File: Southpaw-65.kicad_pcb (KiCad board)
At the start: 2 copper layers, 204 parts, among them J1 USB_C_Receptacle_USB2.0, SW1 SW_Push, U1 ATmega32A-PU, Y1 16MHz

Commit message: Added more diodes into the matrix
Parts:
- moved D0-16 306.8 mm to (420.7, 61.9), turned to 270 degrees
- moved D3-3 282.8 mm to (150.0, 47.6), turned to 270 degrees
- moved D0-11 279.4 mm to (325.4, 61.9), turned to 270 degrees
- moved D0-8 278.8 mm to (268.3, 61.9), turned to 270 degrees
- moved D1-6 270.6 mm to (234.2, 57.1), turned to 270 degrees
- moved D1-7 270.2 mm to (253.2, 57.1), turned to 270 degrees
- moved D0-4 267.8 mm to (192.1, 61.9), turned to 270 degrees
- moved D0-12 266.2 mm to (344.5, 61.9), turned to 270 degrees
- moved D0-10 257.9 mm to (306.4, 61.9), turned to 270 degrees
- moved D1-12 248.2 mm to (348.5, 57.1), turned to 270 degrees
- moved D1-3 245.3 mm to (142.1, 57.1), turned to 270 degrees
- moved D0-5 242.8 mm to (211.1, 61.9), turned to 270 degrees
- moved D1-4 235.9 mm to (196.1, 57.1), turned to 270 degrees
- moved D0-19 230.0 mm to (477.8, 61.9), turned to 270 degrees
- moved D0-6 229.3 mm to (230.2, 61.9), turned to 270 degrees
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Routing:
- net ROW4: track 38.1 -> 57.2 mm
- net ROW3: track 38.1 -> 57.2 mm
- net ROW2: track 38.1 -> 57.2 mm
- net ROW1: track 38.1 -> 57.2 mm
- net ROW0: track 38.1 -> 57.2 mm

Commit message: Finished Diode Matrix
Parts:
- moved D3-19 297.7 mm to (451.6, 47.6), turned to 270 degrees
- moved D2-6 294.2 mm to (238.1, 52.4), turned to 270 degrees
- moved D2-7 287.3 mm to (257.2, 52.4), turned to 270 degrees
- moved D4-8 279.2 mm to (280.2, 47.6), turned to 270 degrees
- moved D4-14 275.7 mm to (386.6, 57.1), turned to 270 degrees
- moved D3-12 275.4 mm to (344.5, 61.9), turned to 270 degrees
- moved D3-8 265.9 mm to (276.2, 52.4), turned to 270 degrees
- moved D4-12 263.7 mm to (348.5, 57.1), turned to 270 degrees
- moved D2-5 259.2 mm to (218.3, 52.4), turned to 270 degrees
- moved D2-10 258.7 mm to (306.4, 61.9), turned to 270 degrees
- moved D4-13 258.3 mm to (368.3, 57.1), turned to 270 degrees
- moved D4-10 255.8 mm to (314.3, 52.4), turned to 270 degrees
- moved D2-8 229.3 mm to (272.3, 57.1), turned to 270 degrees
- moved D3-13 226.7 mm to (364.3, 61.9), turned to 270 degrees
- moved D2-18 219.1 mm to (429.4, 52.4), turned to 270 degrees
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
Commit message: More diodes
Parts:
- moved SW1 394.9 mm to (466.6, 46.2)
- moved C6 341.2 mm to (171.3, 76.2)
- moved C3 339.9 mm to (171.3, 84.1)
- moved C7 329.7 mm to (179.3, 84.1)
- moved R6 314.5 mm to (172.2, 110.6), turned to 270 degrees
- moved R1 290.7 mm to (164.3, 110.6), turned to 270 degrees
- moved C5 279.0 mm to (163.4, 76.2)
- moved Y1 258.1 mm to (174.8, 71.4), turned to 180 degrees
- moved R3 252.7 mm to (180.2, 110.6), turned to 270 degrees
- moved R5 240.0 mm to (176.2, 110.6), turned to 270 degrees
- moved C4 239.5 mm to (179.3, 76.2)
- moved R2 219.9 mm to (168.3, 110.6), turned to 270 degrees
- moved C1 182.2 mm to (163.4, 84.1)
- moved U1 19.0 mm to (164.1, 124.8)
- moved J1 10.2 mm to (176.4, 37.5), turned to 180 degrees
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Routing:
- net ROW0: track 57.2 -> 409.0 mm, vias 0 -> 1
- net ROW1: track 57.2 -> 390.1 mm
- net ROW4: track 57.2 -> 380.1 mm, vias 0 -> 3
- net ROW3: track 57.2 -> 375.6 mm, vias 0 -> 2
- net ROW2: track 57.2 -> 368.4 mm
- net Net-(D4-5-Pad2): track 0.00 -> 145.5 mm
- net Net-(D4-6-Pad2): track 0.00 -> 142.8 mm
- net Net-(D4-8-Pad2): track 0.00 -> 138.2 mm
- net Net-(D4-10-Pad2): track 0.00 -> 137.4 mm
- net Net-(D4-4-Pad2): track 0.00 -> 127.0 mm
- net Net-(D4-3-Pad2): track 0.00 -> 118.3 mm
- net Net-(D4-2-Pad2): track 0.00 -> 118.3 mm
- net Net-(D3-5-Pad2): track 0.00 -> 111.6 mm
- net Net-(D3-6-Pad2): track 0.00 -> 110.8 mm
- net Net-(D3-7-Pad2): track 0.00 -> 110.8 mm
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
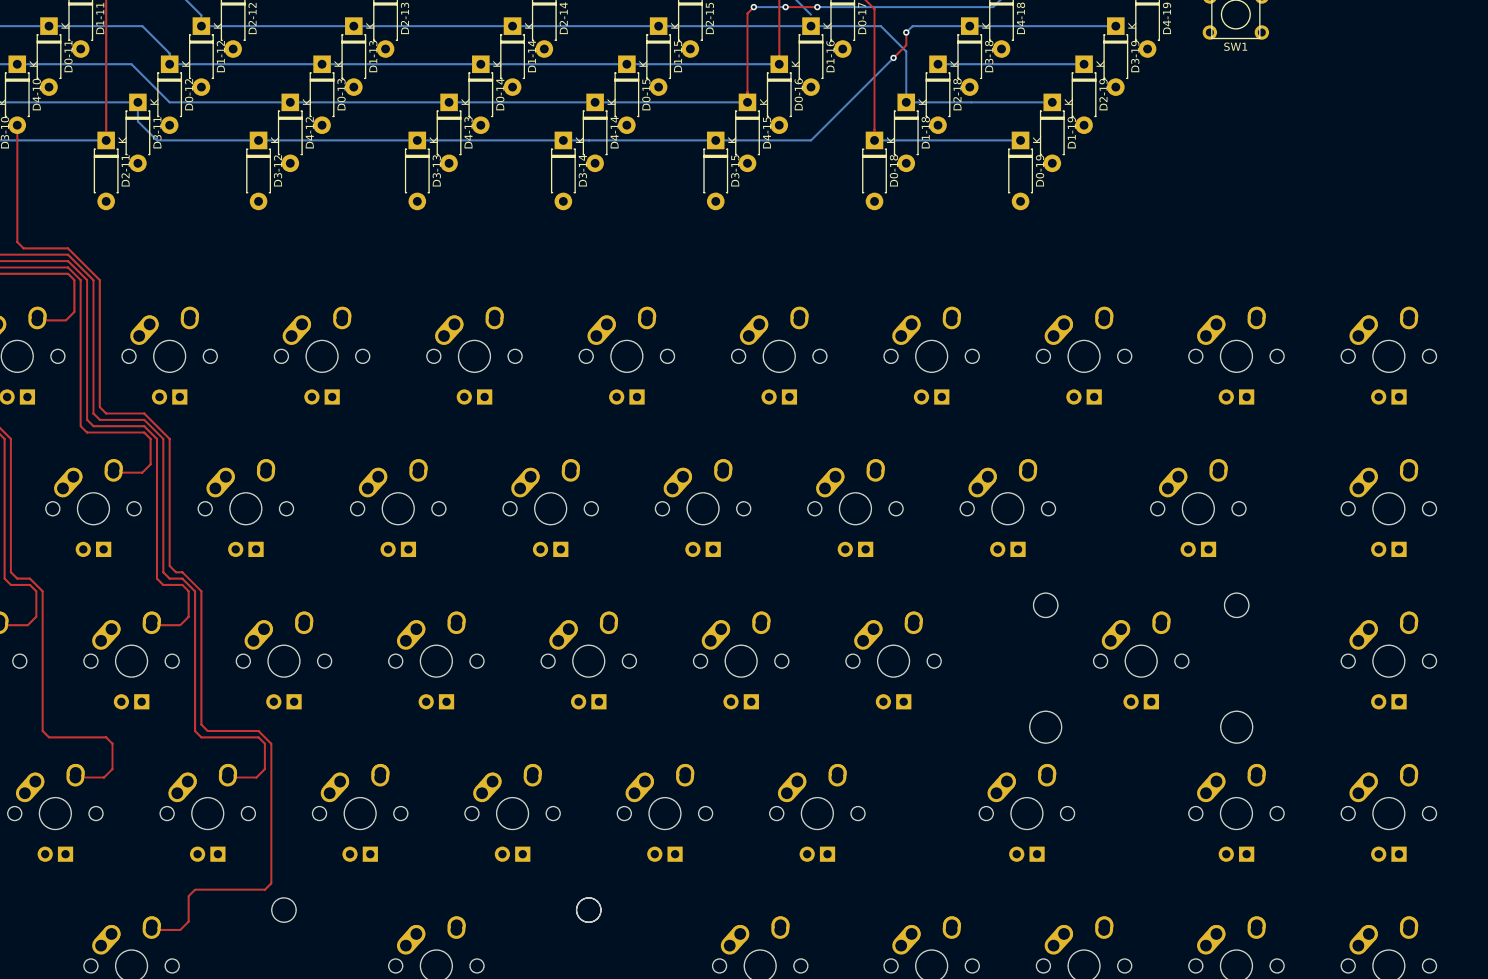
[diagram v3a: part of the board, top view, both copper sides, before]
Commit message: Finished all connections from switches to diodes
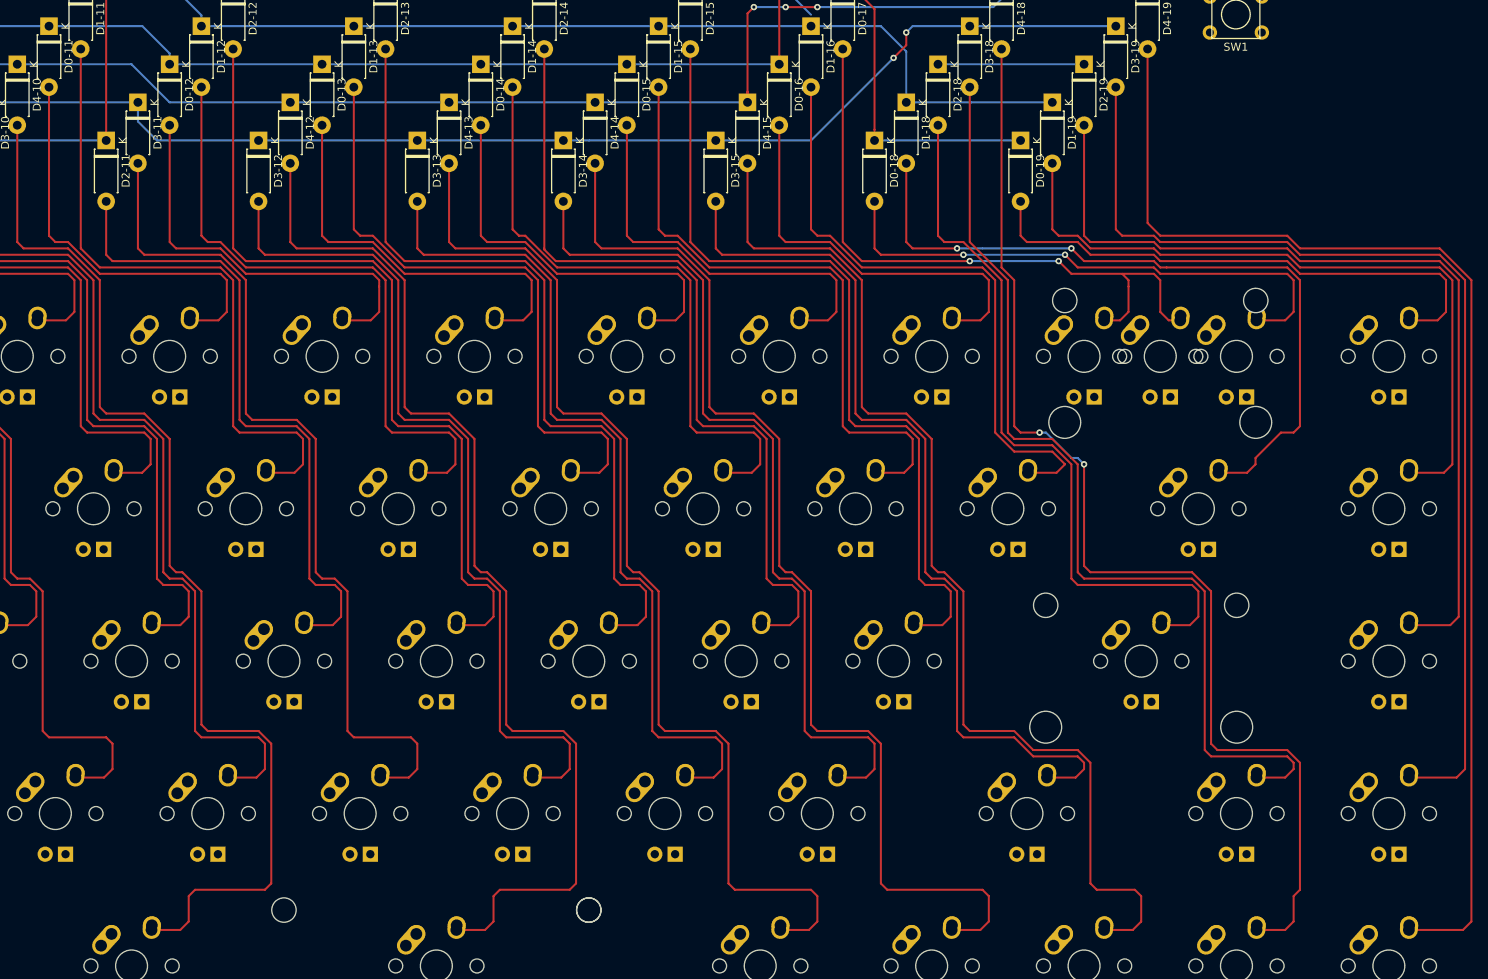
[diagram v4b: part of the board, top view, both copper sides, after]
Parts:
- added MX0-17B1: MX-NoLED, MX_Alps_Hybrid:MX-2U, F.Cu at (457.2, 88.9)
- renumbered MX0-17 to MX0-17A1
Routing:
- net Net-(D4-19-Pad2): track 0.00 -> 153.6 mm
- net Net-(D4-18-Pad2): track 0.00 -> 144.8 mm, vias 0 -> 2
- net Net-(D4-14-Pad2): track 0.00 -> 139.8 mm
- net Net-(D4-15-Pad2): track 0.00 -> 138.4 mm
- net Net-(D4-12-Pad2): track 0.00 -> 136.6 mm
- net Net-(D4-13-Pad2): track 0.00 -> 136.6 mm
- net Net-(D3-19-Pad2): track 0.00 -> 132.6 mm
- net Net-(D3-18-Pad2): track 0.00 -> 123.4 mm
- net Net-(D3-15-Pad2): track 0.00 -> 114.2 mm
- net Net-(D2-19-Pad2): track 0.00 -> 111.7 mm
- net Net-(D3-11-Pad2): track 0.00 -> 109.2 mm
- net Net-(D3-14-Pad2): track 0.00 -> 108.4 mm
- net Net-(D3-12-Pad2): track 0.00 -> 108.4 mm
- net Net-(D3-13-Pad2): track 0.00 -> 107.6 mm
- net Net-(D2-12-Pad2): track 0.00 -> 103.9 mm
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
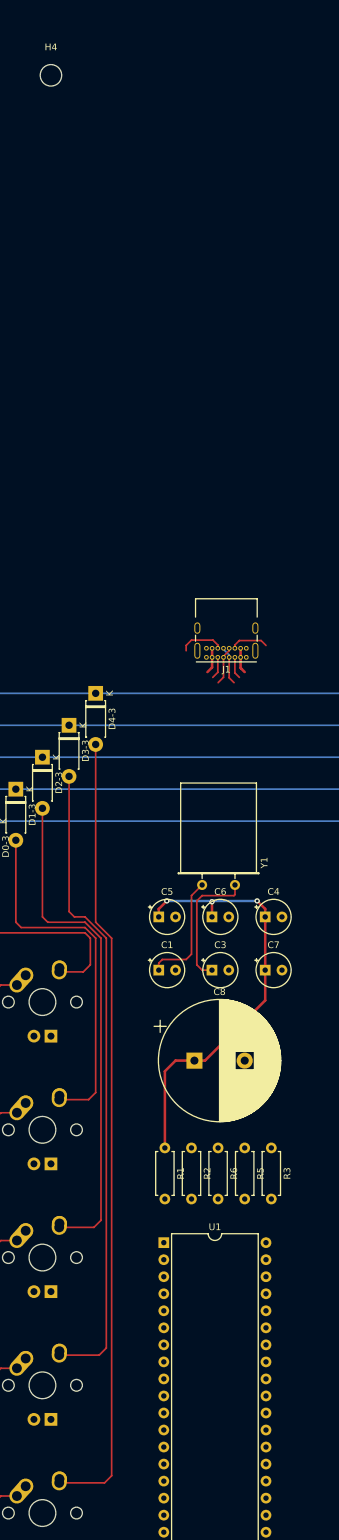
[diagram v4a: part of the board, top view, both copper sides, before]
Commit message: Started routing the wiring for the capacitors and diodes
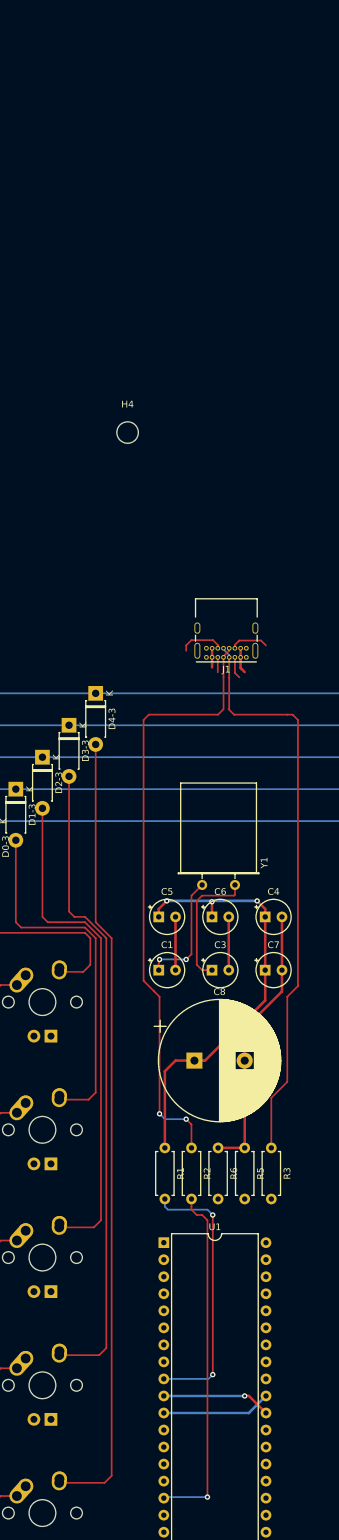
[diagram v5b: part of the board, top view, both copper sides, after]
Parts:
- moved H4 54.5 mm to (158.8, 3.97)
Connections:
- U1 pad 1: COL3 -> Net-(U1-Pad1)
- U1 pad 14: COL19 -> Net-(U1-Pad14)
- U1 pad 2: COL4 -> Net-(U1-Pad2)
- U1 pad 22: COL11 -> Net-(U1-Pad22)
- U1 pad 23: COL12 -> Net-(U1-Pad23)
- U1 pad 24: COL13 -> Net-(U1-Pad24)
- U1 pad 25: COL14 -> Net-(U1-Pad25)
- U1 pad 26: COL15 -> Net-(U1-Pad26)
- U1 pad 27: COL16 -> Net-(U1-Pad27)
- U1 pad 28: COL17 -> Net-(U1-Pad28)
- U1 pad 29: COL18 -> Net-(U1-Pad29)
- U1 pad 3: COL5 -> Net-(U1-Pad3)
- U1 pad 33: COL2 -> Net-(U1-Pad33)
- U1 pad 34: COL1 -> Net-(U1-Pad34)
- U1 pad 35: COL0 -> Net-(U1-Pad35)
- U1 pad 36: ROW4 -> Net-(U1-Pad36)
- U1 pad 37: ROW3 -> Net-(U1-Pad37)
- U1 pad 38: ROW2 -> Net-(U1-Pad38)
- U1 pad 39: ROW1 -> Net-(U1-Pad39)
- U1 pad 4: COL6 -> Net-(U1-Pad4)
- U1 pad 40: ROW0 -> Net-(U1-Pad40)
- U1 pad 5: COL7 -> Net-(U1-Pad5)
- U1 pad 6: COL8 -> Net-(U1-Pad6)
- U1 pad 7: COL9 -> Net-(U1-Pad7)
- U1 pad 8: COL10 -> Net-(U1-Pad8)
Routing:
- net D-: track 5.82 -> 90.6 mm, vias 0 -> 2
- net D+: track 5.78 -> 85.9 mm
- net GND: track 0.00 -> 72.9 mm
- net Net-(R2-Pad2): track 0.00 -> 52.5 mm, vias 0 -> 1
- net Reset: track 0.00 -> 40.2 mm, vias 0 -> 2
- net +5V: track 72.3 -> 87.7 mm, vias 3 -> 4
- net Net-(J1-PadA8): track 3.30 -> 2.24 mm
- net C16: track 17.5 -> 17.7 mm, vias 0 -> 2

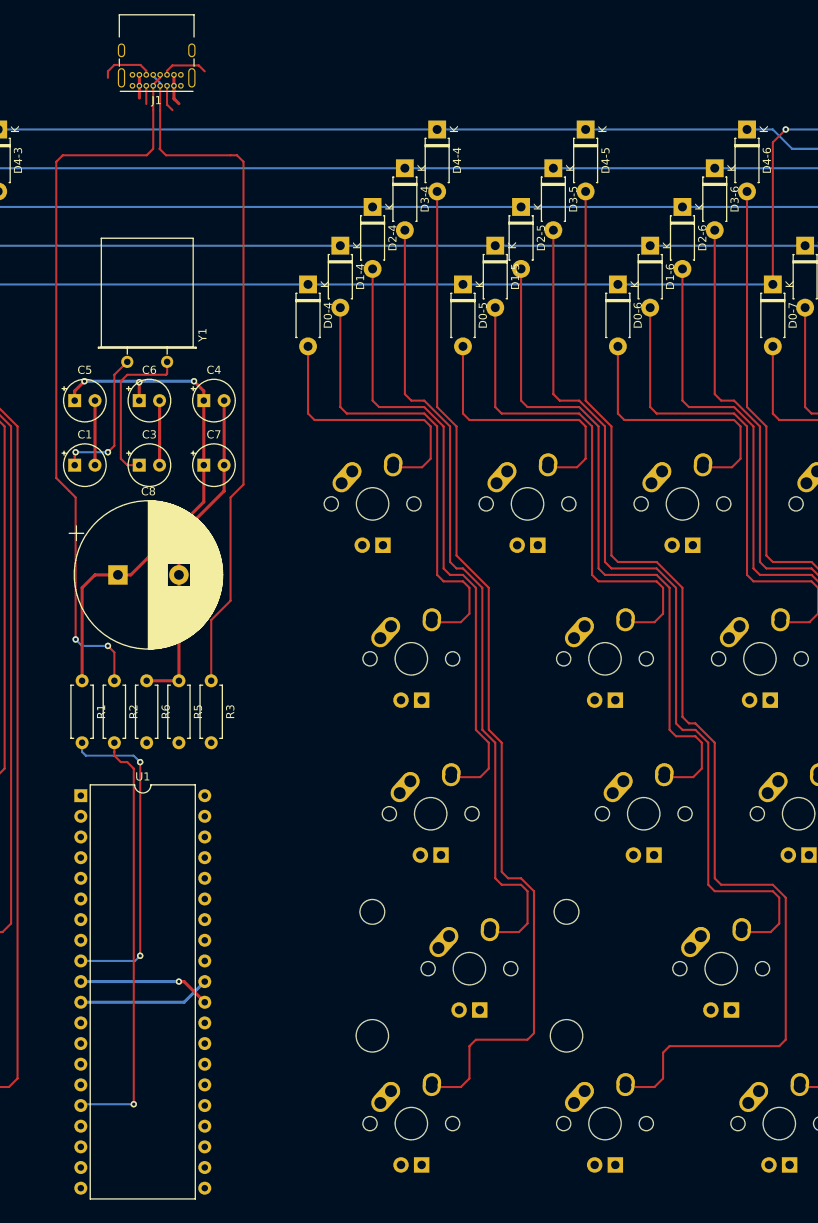
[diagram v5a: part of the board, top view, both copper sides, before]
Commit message: Wiring switches together
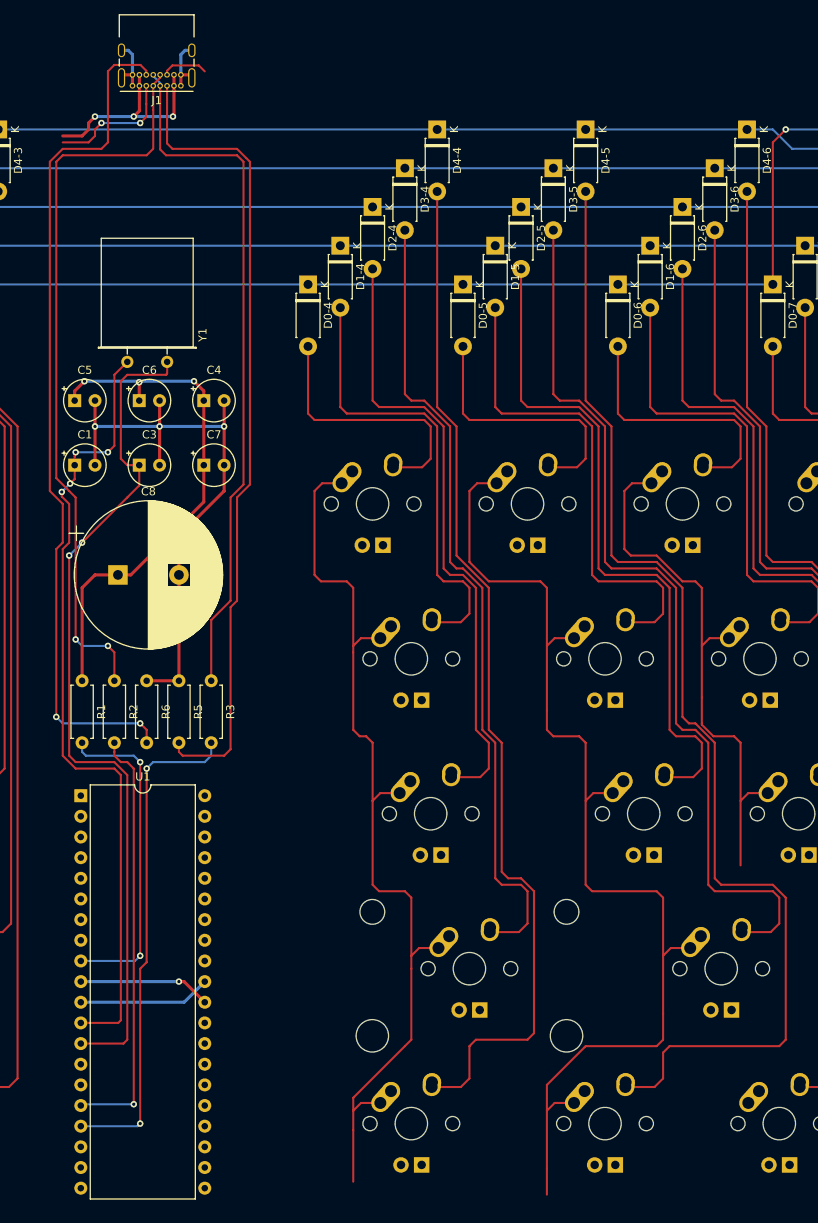
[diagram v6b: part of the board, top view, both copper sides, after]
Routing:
- net COL5: track 0.00 -> 136.3 mm
- net COL4: track 0.00 -> 115.6 mm
- net Net-(J1-PadB5): track 6.64 -> 105.3 mm, vias 0 -> 2
- net Net-(J1-PadA5): track 3.27 -> 99.4 mm
- net C17: track 19.6 -> 105.5 mm, vias 0 -> 2
- net C16: track 17.7 -> 98.1 mm, vias 2 -> 4
- net COL6: track 0.00 -> 67.4 mm
- net Net-(R3-Pad2): track 0.00 -> 61.6 mm, vias 0 -> 2
- net GND: track 72.9 -> 102.6 mm, vias 0 -> 3
- net +5V: track 87.7 -> 106.6 mm, vias 4 -> 7
- net Net-(J1-PadA8): track 2.24 -> 15.9 mm, vias 0 -> 2

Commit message: Did more wiring
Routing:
- net COL14: track 0.00 -> 135.8 mm
- net COL15: track 0.00 -> 135.4 mm
- net COL13: track 0.00 -> 133.9 mm
- net COL7: track 0.00 -> 133.8 mm
- net COL10: track 0.00 -> 133.0 mm
- net COL12: track 0.00 -> 132.9 mm
- net COL8: track 0.00 -> 132.1 mm
- net COL9: track 0.00 -> 132.1 mm
- net COL11: track 0.00 -> 131.4 mm
- net COL16: track 0.00 -> 119.5 mm, vias 0 -> 2
- net COL18: track 0.00 -> 101.8 mm, vias 0 -> 2
- net COL6: track 67.4 -> 133.5 mm

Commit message: Just a backup
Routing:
- net GND: track 102.6 -> 444.5 mm, vias 3 -> 6
- net Reset: track 40.2 -> 312.9 mm, vias 2 -> 3
- net COL17: track 0.00 -> 123.1 mm, vias 0 -> 2
- net COL19: track 0.00 -> 105.2 mm
- net +5V: track 106.6 -> 192.3 mm, vias 7 -> 11
- net COL18: track 101.8 -> 126.2 mm
- net ROW2: track 368.4 -> 389.6 mm, vias 0 -> 1
